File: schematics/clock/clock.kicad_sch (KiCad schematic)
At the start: 8 parts, among them U1 LM555xM

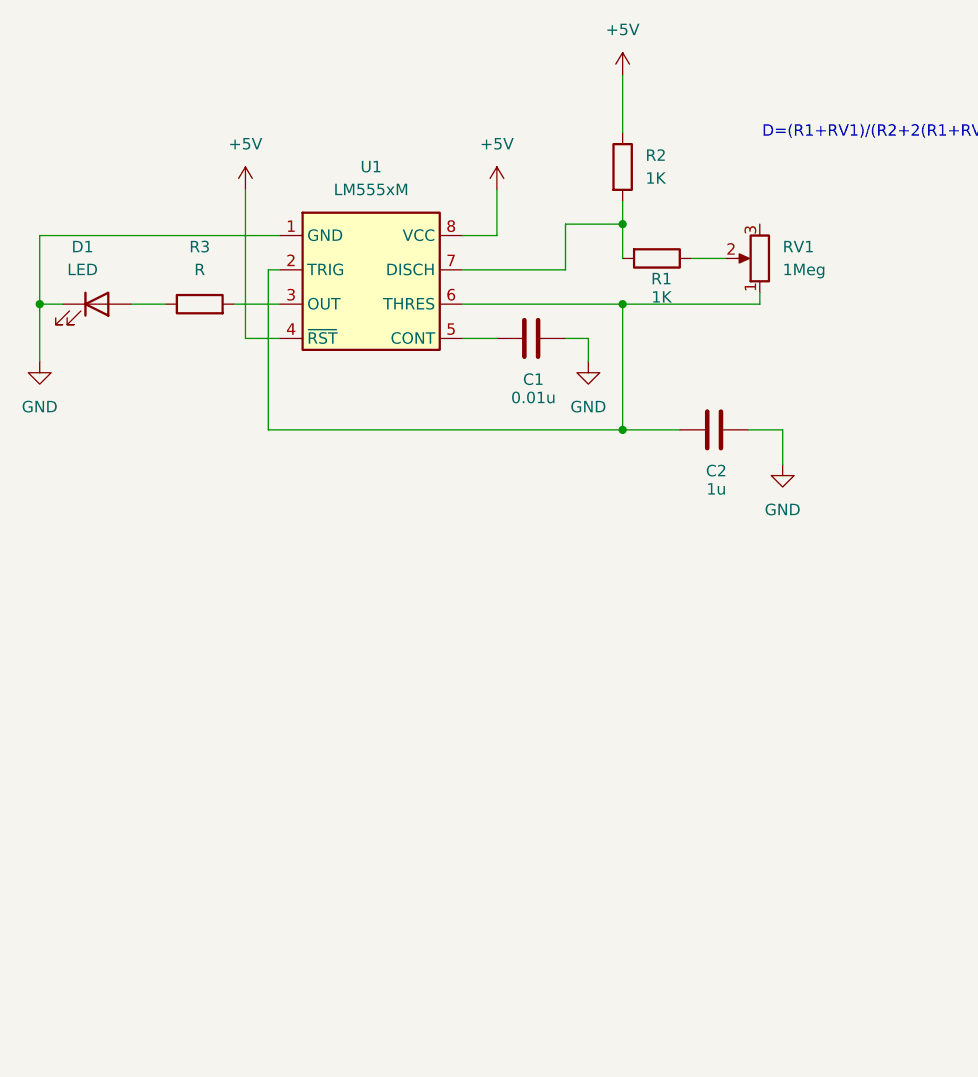
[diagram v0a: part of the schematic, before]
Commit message: add debouncing
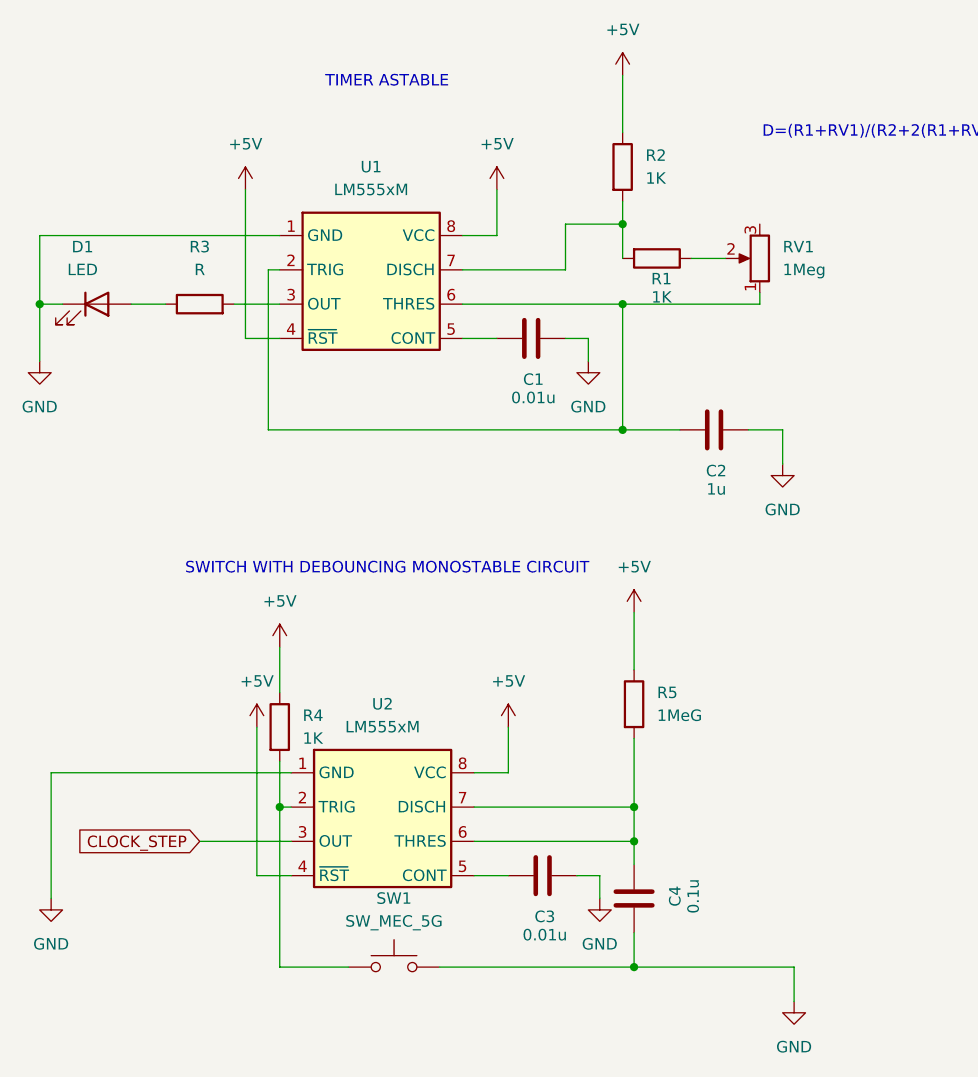
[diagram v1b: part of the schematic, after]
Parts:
- added C3: 0.01u, symbol Device:C
- added C4: 0.1u, symbol Device:C
- added R4: 1K, symbol Device:R
- added R5: 1MeG, symbol Device:R
- added SW1: SW_MEC_5G, symbol Switch:SW_MEC_5G
- added U2: LM555xM, Package_SO:SOIC-8_3.9x4.9mm_P1.27mm, symbol breadboard:LM555xM
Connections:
- net +5V: now also R4.1, R5.1, U2.4 (~{RST}), U2.8 (VCC)
- net GND: now also C3.2, C4.1, SW1.3 (B), SW1.4 (B), U2.1 (GND)
- new net: R4.2, SW1.1 (A), SW1.2 (A), U2.2 (TRIG)
- new net: C4.2, R5.2, U2.6 (THRES), U2.7 (DISCH)
- new net: C3.1, U2.5 (CONT)
- new net CLOCK_STEP: U2.3 (OUT)
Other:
- note added: "SWITCH WITH DEBOUNCING MONOSTABLE CIRCUIT"
- note added: "TIMER ASTABLE"

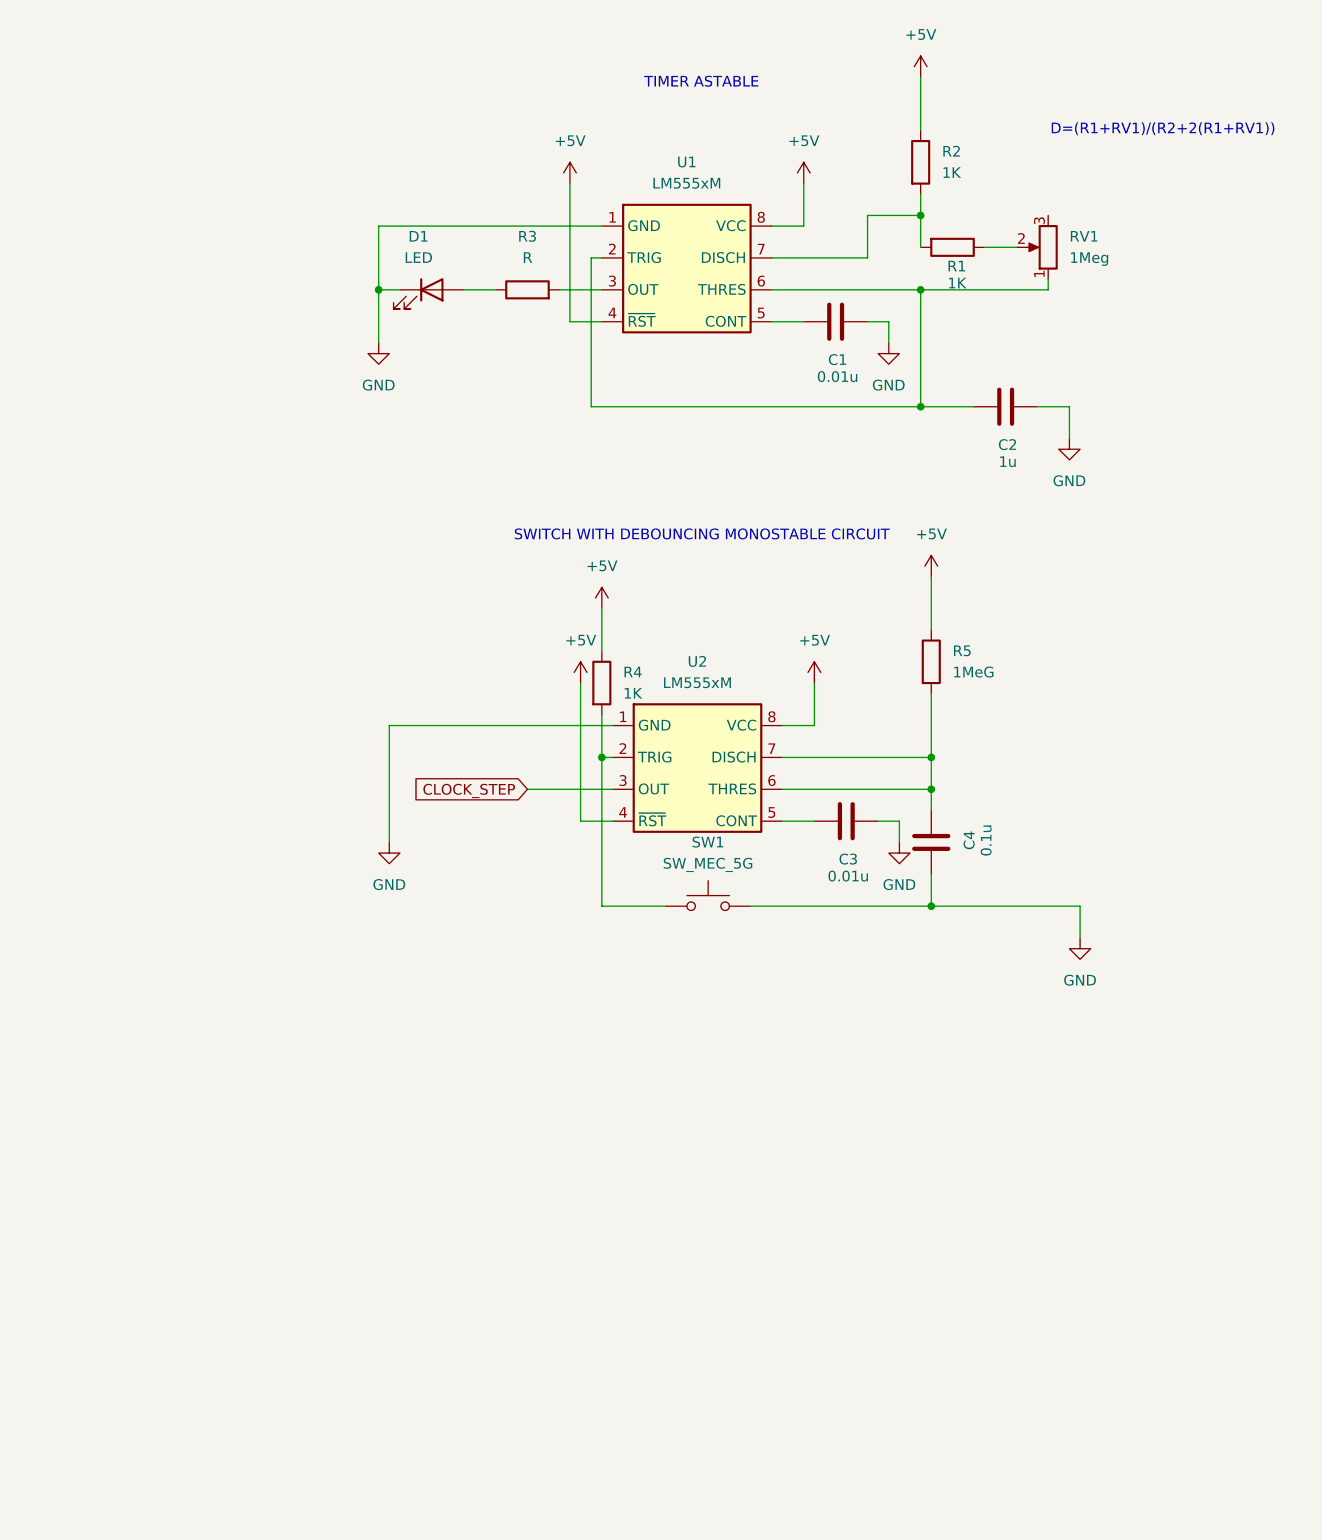
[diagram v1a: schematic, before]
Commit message: reformat for hierarchy
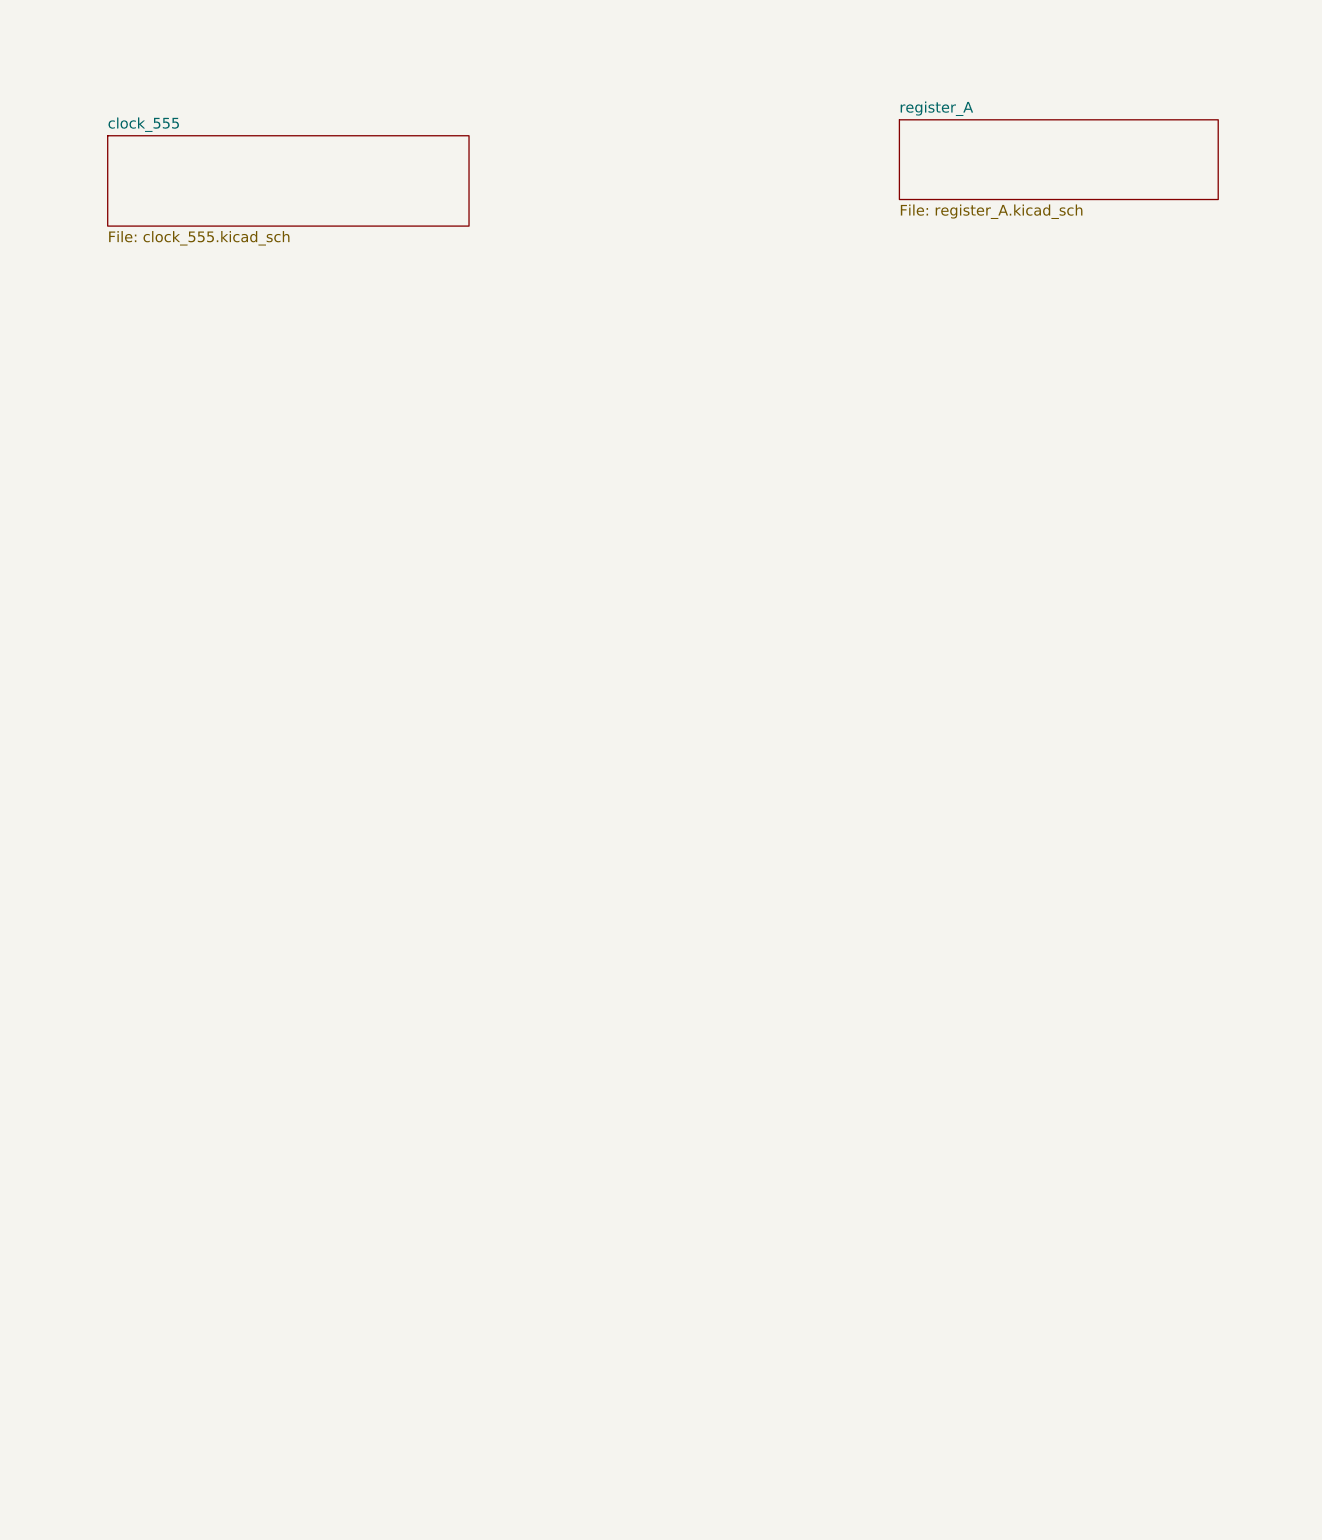
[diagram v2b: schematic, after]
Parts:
- removed C1, C3: 0.01u, symbol Device:C
- removed C2: 1u, symbol Device:C
- removed C4: 0.1u, symbol Device:C
- removed D1: LED, symbol Device:LED
- removed R1, R2, R4: 1K, symbol Device:R
- removed R3: R, symbol Device:R
- removed R5: 1MeG, symbol Device:R
- removed RV1: 1Meg, symbol Device:R_Potentiometer
- removed SW1: SW_MEC_5G, symbol Switch:SW_MEC_5G
- removed U1, U2: LM555xM, Package_SO:SOIC-8_3.9x4.9mm_P1.27mm, symbol breadboard:LM555xM
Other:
- added sheet clock_555 (clock_555.kicad_sch)
- added sheet register_A (register_A.kicad_sch)
- note removed: "D=(R1+RV1)/(R2+2(R1+RV1))"
- note removed: "SWITCH WITH DEBOUNCING MONOSTABLE CIRCUIT"
- note removed: "TIMER ASTABLE"

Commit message: add change mode case
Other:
- added sheet bus (bus.kicad_sch)
- added sheet memory_register (memory_register.kicad_sch)
- added sheet register_B (register_B.kicad_sch)
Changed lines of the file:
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@@
 	(generator_version "9.0")
 	(paper "A4")
+	(global_label "~{CLK}"
+		(shape input)
+		(at 50.8 43.18 180)
+		(fields_autoplaced yes)
+		(effects
+			(font
+				(size 1.27 1.27)
+			)
+			(justify right)
+		)
+		(property "Intersheetrefs" "${INTERSHEET_REFS}"
+			(at 44.2467 43.18 0)
+			(effects
+				(font
+					(size 1.27 1.27)
+				)
+				(justify right)
+				(hide yes)
+			)
+		)
+	)
+	(global_label "CLK"
+		(shape input)
+		(at 50.8 38.1 180)
+		(fields_autoplaced yes)
+		(effects
+			(font
+				(size 1.27 1.27)
+			)
+			(justify right)
+		)
+		(property "Intersheetrefs" "${INTERSHEET_REFS}"
+			(at 44.2467 38.1 0)
+			(effects
+				(font
+					(size 1.27 1.27)
+				)
+				(justify right)
+				(hide yes)
+			)
+		)
+	)
+	(sheet
+		(at 139.065 78.105)
+		(size 41.275 13.97)
+		(exclude_from_sim no)
+		(in_bom yes)
+		(on_board yes)
+		(dnp no)
+		(fields_autoplaced yes)
+		(stroke
+			(width 0.1524)
+			(type solid)
+		)
+		(fill
+			(color 0 0 0 0.0000)
+		)
+		(property "Sheetname" "memory_register"
+			(at 139.065 77.3934 0)
+			(effects
+				(font
+					(size 1.27 1.27)
+				)
+				(justify left bottom)
+			)
+		)
+		(property "Sheetfile" "memory_register.kicad_sch"
+			(at 139.065 92.6596 0)
+			(effects
+				(font
+					(size 1.27 1.27)
+				)
+				(justify left top)
+			)
+		)
+		(instances
+			(project "clock"
+				(path "/1be175cd-1437-4d72-8152-541f02e1a99b"
+					(page "9")
+				)
+			)
+		)
+	)
+	(sheet
+		(at 138.43 56.515)
+		(size 39.37 13.97)
+		(exclude_from_sim no)
+		(in_bom yes)
+		(on_board yes)
+		(dnp no)
+		(fields_autoplaced yes)
+		(stroke
+			(width 0.1524)
+			(type solid)
+		)
+		(fill
+			(color 0 0 0 0.0000)
+		)
+		(property "Sheetname" "register_B"
+			(at 138.43 55.8034 0)
+			(effects
+				(font
+					(size 1.27 1.27)
+				)
+				(justify left bottom)
+			)
+		)
+		(property "Sheetfile" "register_B.kicad_sch"
+			(at 138.43 71.0696 0)
+			(effects
+				(font
+					(size 1.27 1.27)
+				)
+				(justify left top)
+			)
+		)
+		(instances
+			(project "clock"
+				(path "/1be175cd-1437-4d72-8152-541f02e1a99b"
+					(page "8")
+				)
+			)
+		)
+	)
+	(sheet
+		(at 88.265 36.83)
+		(size 17.145 57.15)
+		(exclude_from_sim no)
+		(in_bom yes)
+		(on_board yes)
+		(dnp no)
+		(fields_autoplaced yes)
+		(stroke
+			(width 0.1524)
+			(type solid)
+		)
+		(fill
+			(color 0 0 0 0.0000)
+		)
+		(property "Sheetname" "bus"
+			(at 88.265 36.1184 0)
+			(effects
+				(font
+					(size 1.27 1.27)
+				)
+				(justify left bottom)
+			)
+		)
+		(property "Sheetfile" "bus.kicad_sch"
+			(at 88.265 94.5646 0)
+			(effects
+				(font
+					(size 1.27 1.27)
+				)
+				(justify left top)
+			)
+		)
+		(instances
+			(project "clock"
+				(path "/1be175cd-1437-4d72-8152-541f02e1a99b"
+					(page "7")
+				)
+			)
+		)
+	)
 	(sheet
 		(at 42.545 34.925)
-		(size 43.18 10.795)
+		(size 12.7 10.795)
 		(exclude_from_sim no)
 		(in_bom yes)
